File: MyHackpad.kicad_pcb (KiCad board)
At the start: 2 copper layers, 92.2 x 62.8 mm, 17 parts, among them J1 OLED_128x32, SW1 RotaryEncoder_Switch, U1 MOUDLE-SEEEDUINO-XIAO

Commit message: Added LEDs to the Schematic
Added some SK6812 MINI-E LEDs to the shcematic and tidied up all connections
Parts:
- added D10: SK6812MINI-E, LED_SMD:LED_SK6812MINI-E_3.2x2.8mm_P1.5mm_ReverseMount, F.Cu at (226.0, 101.0)
- added D11: SK6812MINI-E, LED_SMD:LED_SK6812MINI-E_3.2x2.8mm_P1.5mm_ReverseMount, F.Cu at (226.0, 105.9)
- added D12: SK6812MINI-E, LED_SMD:LED_SK6812MINI-E_3.2x2.8mm_P1.5mm_ReverseMount, F.Cu at (226.0, 110.8)
- added D7: SK6812MINI-E, LED_SMD:LED_SK6812MINI-E_3.2x2.8mm_P1.5mm_ReverseMount, F.Cu at (226.0, 86.4)
- added D8: SK6812MINI-E, LED_SMD:LED_SK6812MINI-E_3.2x2.8mm_P1.5mm_ReverseMount, F.Cu at (226.0, 91.3)
- added D9: SK6812MINI-E, LED_SMD:LED_SK6812MINI-E_3.2x2.8mm_P1.5mm_ReverseMount, F.Cu at (226.0, 96.2)
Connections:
- net Column 0 renamed COLUMN_0
- net Column 1 renamed COLUMN_1
- net Column 2 renamed COLUMN_2
- net ENCODER A renamed ENCODER_A
- net ENCODER B renamed ENCODER_B
- net ENCODER S1 renamed ENCODER_S1
- net OLED SCL renamed OLED_SCL
- net OLED SDA renamed OLED_SDA
- net OLED VCC renamed OLED_VCC
- net Row 0 renamed ROW_0
- net Row 1 renamed ROW_1
- U1 pad 14: unconnected-(U1-5V-Pad14) -> LEDs_VDD
- U1 pad 8: unconnected-(U1-PB09_A7_D7_RX-Pad8) -> LEDs_DIN

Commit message: Added LEDs to PCB (hopefully)
Should have added LEDs to the PCB in the right way? Still waiting for answers from the slack. Could change in the future.
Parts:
- added G***: LOGO, my_logos:hackclub_silkscreen_15x5.2mm, B.Cu at (190.5, 53.0)
- moved D7 92.8 mm to (133.3, 80.4)
- moved D10 92.6 mm to (133.3, 99.4)
- moved D8 74.4 mm to (152.4, 80.4)
- moved D11 73.8 mm to (152.4, 99.4)
- moved D9 56.7 mm to (171.4, 80.4)
- moved D12 55.7 mm to (171.4, 99.4)
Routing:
- net LEDs_VDD: track 0.00 -> 179.0 mm, vias 0 -> 13
- net GND: track 117.9 -> 262.3 mm, vias 0 -> 8
- net LEDs_DIN: track 0.00 -> 71.1 mm, vias 0 -> 2
- net Net-(D10-DIN): track 0.00 -> 61.2 mm, vias 0 -> 4
- net Net-(D10-DOUT): track 0.00 -> 15.2 mm, vias 0 -> 2
- net Net-(D7-DOUT): track 0.00 -> 14.7 mm, vias 0 -> 2
- net Net-(D8-DOUT): track 0.00 -> 14.2 mm, vias 0 -> 2
- net Net-(D11-DOUT): track 0.00 -> 14.2 mm
- net ROW_1: track 62.1 -> 71.2 mm, vias 0 -> 2
- net ROW_0: track 58.9 -> 65.8 mm
- net COLUMN_1: track 69.9 -> 73.2 mm
- net COLUMN_0: track 91.8 -> 95.0 mm
- net COLUMN_2: track 47.1 -> 50.4 mm
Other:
- board size 92.2 x 62.8 mm -> 95 x 60.8 mm
- board text added: "This space kinda empty"

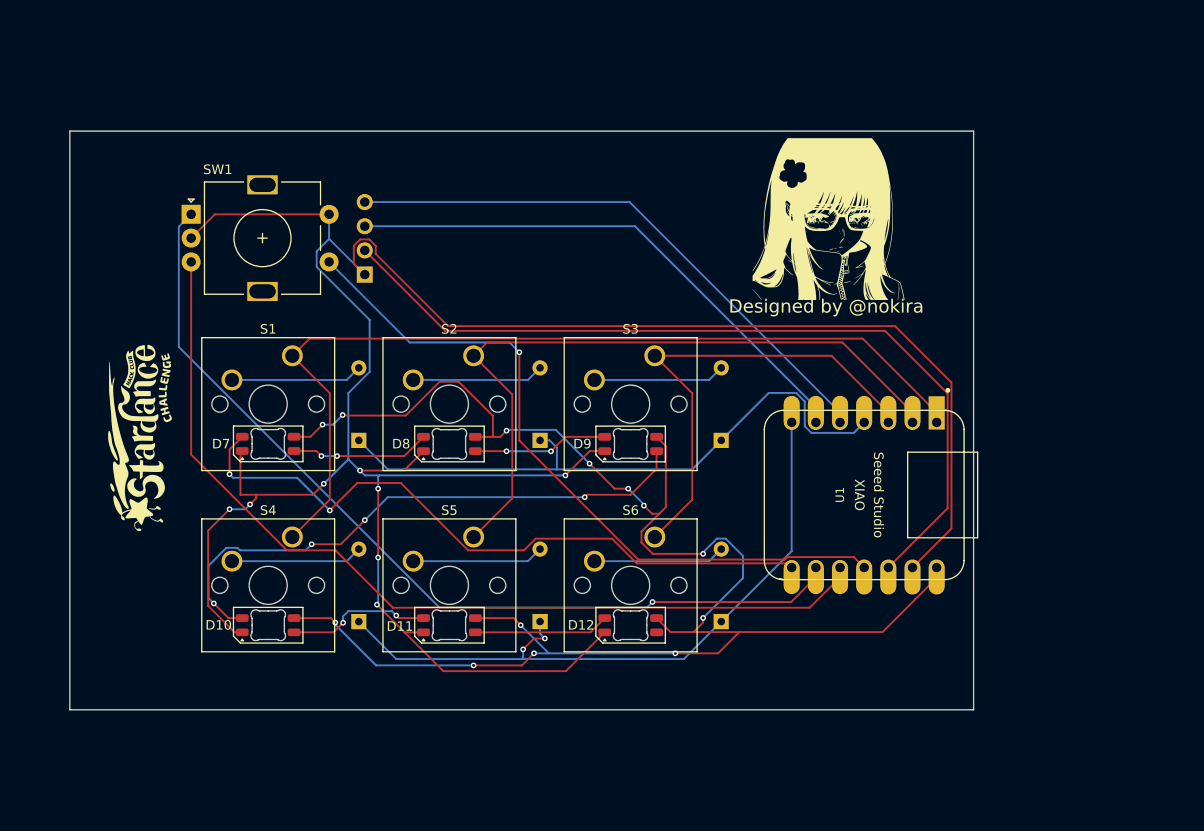
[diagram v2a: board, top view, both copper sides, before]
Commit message: Placed LEDs correctly on the board
Placed the LEDs thanks to the help found in the Slack channel. Also routed the board from zero because it was quite messy. Now it should be clear :)
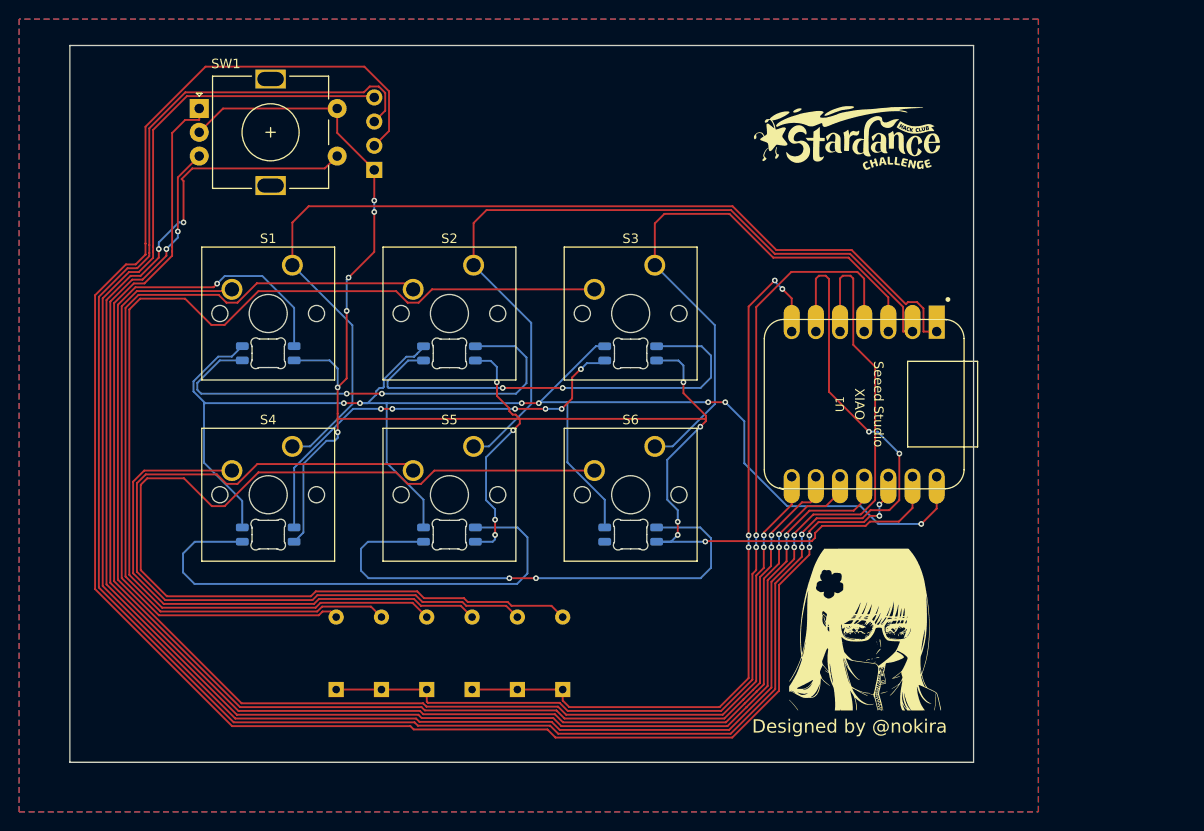
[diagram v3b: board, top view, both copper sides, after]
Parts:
- D10, D11, D12, D7, D8, D9: moved to B.Cu
- moved G*** 80.9 mm to (194.2, 48.1), turned to 0 degrees
- moved G*** 43.3 mm to (196.6, 99.9)
- moved D3 40.6 mm to (150.0, 106.2)
- moved D2 31.0 mm to (145.3, 106.2)
- moved D1 26.3 mm to (140.5, 106.2)
- moved D6 18.1 mm to (164.3, 106.2)
- moved G*** 17.3 mm to (176.0, 43.6)
- moved D4 13.9 mm to (154.8, 106.2)
- moved SW1 11.2 mm to (126.1, 45.1)
- moved J1 11.0 mm to (142.9, 41.8)
- moved U1 9.55 mm to (196.0, 76.2)
- moved D10 9.53 mm to (133.3, 89.9), turned to 180 degrees
- moved D11 9.53 mm to (152.4, 89.9), turned to 180 degrees
- moved D12 9.53 mm to (171.4, 89.9), turned to 180 degrees
- moved D7 9.53 mm to (133.3, 70.9), turned to 180 degrees
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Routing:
- net OLED_SCL: track 56.9 -> 224.3 mm, vias 0 -> 4
- net OLED_SDA: track 60.2 -> 212.5 mm, vias 0 -> 2
- net OLED_VCC: track 88.4 -> 198.1 mm, vias 0 -> 4
- net Net-(D3-A): track 13.9 -> 114.5 mm
- net ENCODER_S1: track 75.2 -> 170.7 mm, vias 1 -> 4
- net Net-(D6-A): track 13.9 -> 107.5 mm
- net LEDs_DIN: track 71.1 -> 151.6 mm, vias 2 -> 3
- net Net-(D2-A): track 13.9 -> 89.6 mm
- net Net-(D5-A): track 13.9 -> 82.7 mm
- net GND: track 262.3 -> 196.7 mm, vias 8 -> 15
- net ENCODER_A: track 95.2 -> 155.0 mm, vias 1 -> 2
- net ENCODER_B: track 97.5 -> 152.1 mm, vias 0 -> 4
- net Net-(D1-A): track 13.9 -> 65.7 mm
- net Net-(D4-A): track 13.9 -> 58.5 mm
- net Net-(D11-DOUT): track 14.2 -> 56.1 mm, vias 0 -> 2
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- added copper zone on B.Cu, net (none)
- added copper zone on F.Cu, net (none)
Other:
- board size 95 x 60.8 mm -> 95 x 75.3 mm
